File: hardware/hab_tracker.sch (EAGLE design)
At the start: 40 parts, among them IC1 LD117AV33, J3 GP-735T-VERTICAL, U1 ATMEGA328P_TQFP, U2 TMP102, U3 MPL3115A2, U4 9DoF IMU

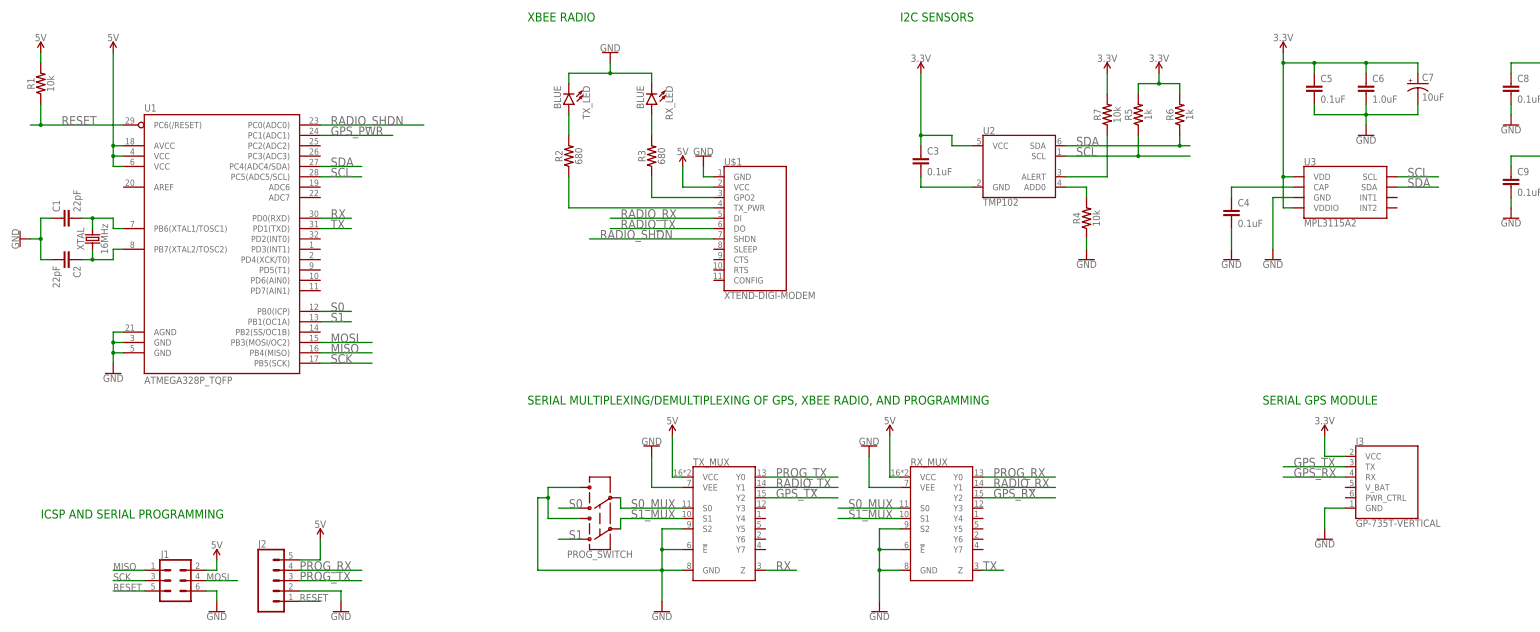
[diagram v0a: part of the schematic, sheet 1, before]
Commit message: Updated schematic and removed schematic history
Removed unnecessary schematic history files generated by Eagle. Also
changed from ATMEGA328p to ATMEGA2561. This allows for removal of serial
MUX circuitry as there are 2 UART ports on the ATMEGA2561 chip. This
will greatly simplify both the hardware and the firmware. Also, removed
serial programming capability. All programming will be done over JTAG
using AVR Pocket Programmer.
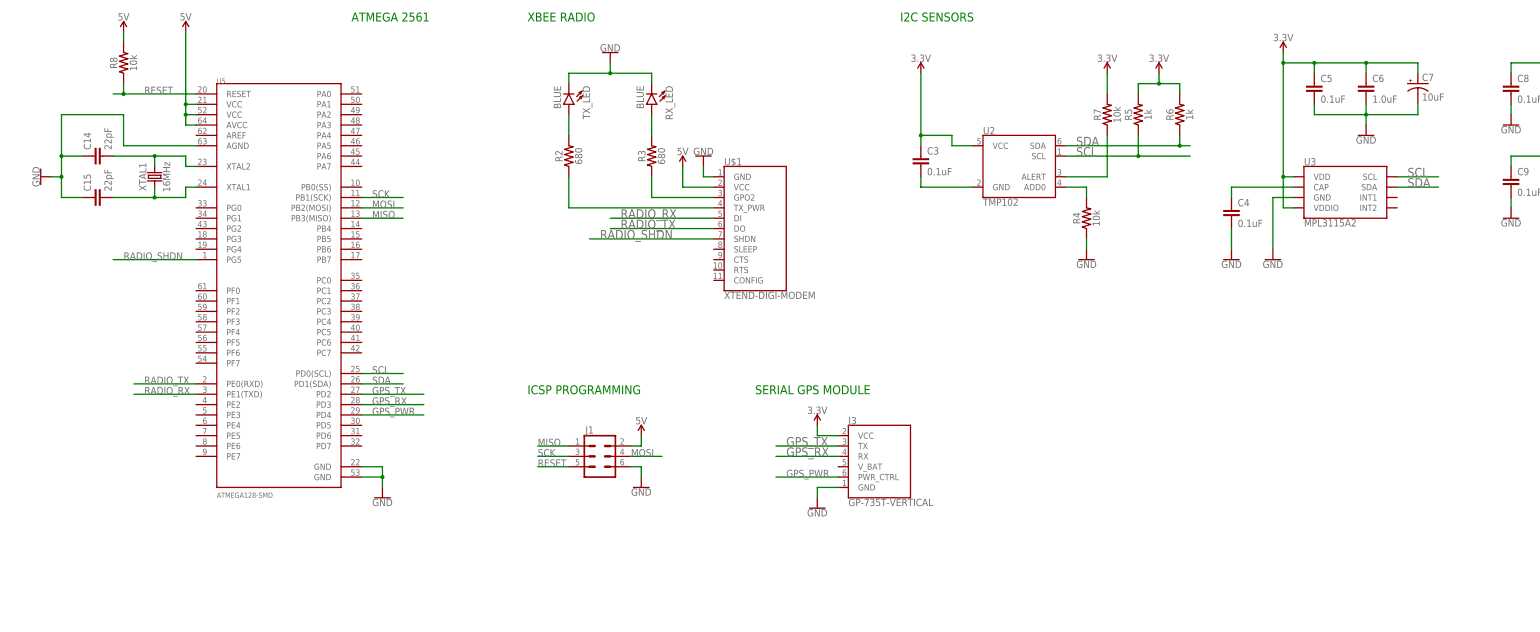
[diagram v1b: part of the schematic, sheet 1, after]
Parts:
- removed C1, C2: 22pF, SparkFun-Capacitors:22PF-0603-50V-5%
- removed J2: (no value), SparkFun-Connectors:CONN_05LOCK
- removed PROG_SWITCH: (no value), SparkFun-Switches:SWITCH-DPDT-SMD-AYZ0202
- removed R1: 10k, SparkFun-Resistors:10KOHM-0603-1/10W-1%
- removed RX_MUX, TX_MUX: (no value), SparkFun-IC-Logic:74HC4051BQ
- removed U1: ATMEGA328P_TQFP, SparkFun-IC-Microcontroller:ATMEGA328P_TQFP
- removed XTAL: 16MHz, SparkFun-Clocks:CRYSTAL-16MHZSMD-5X3.2
- added C14, C15: 22pF, SparkFun-Capacitors:22PF-0603-50V-5%
- added R8: 10k, SparkFun-Resistors:10KOHM-0603-1/10W-1%
- added U5: ATMEGA128-SMD, SparkFun-IC-Microcontroller:ATMEGA128-SMD
- added XTAL1: 16MHz, SparkFun-Clocks:CRYSTAL-16MHZSMD-5X3.2
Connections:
- removed net N$1: C1.2, U1.PB6(XTAL1/TOSC1), XTAL.2
- removed net N$2: C2.1, U1.PB7(XTAL2/TOSC2), XTAL.1
- removed net PROG_RX: J2.4, RX_MUX.Y0
- removed net PROG_TX: J2.3, TX_MUX.Y0
- removed net RX: TX_MUX.Z, U1.PD0(RXD)
- removed net S0: PROG_SWITCH.4, U1.PB0(ICP)
- removed net S0_MUX: PROG_SWITCH.5, RX_MUX.S0, TX_MUX.S0
- removed net S1: PROG_SWITCH.1, U1.PB1(OC1A)
- removed net S1_MUX: PROG_SWITCH.2, RX_MUX.S1, TX_MUX.S1
- removed net TX: RX_MUX.Z, U1.PD1(TXD)
- new net N$16: C14.2, U5.XTAL2, XTAL1.2
- new net N$17: C15.2, U5.XTAL1, XTAL1.1
- net 5V: now also R8.2, U5.AVCC, U5.VCC@21, U5.VCC@52; no longer J2.5, R1.2, RX_MUX.VCC, TX_MUX.VCC, U1.AVCC, U1.VCC@4, U1.VCC@6
- net GND: now also C14.1, C15.1, U5.AGND, U5.GND@22, U5.GND@53; no longer C1.1, C2.2, J2.2, PROG_SWITCH.3, PROG_SWITCH.6, RX_MUX.!E!, RX_MUX.GND, RX_MUX.S2, RX_MUX.VEE, TX_MUX.!E!, TX_MUX.GND, TX_MUX.S2, TX_MUX.VEE, U1.AGND, U1.GND@3, U1.GND@5
- net GPS_PWR: now also J3.PWR_CTRL, U5.PD4; no longer U1.PC1(ADC1)
- net GPS_RX: now also U5.PD3; no longer RX_MUX.Y2
- net GPS_TX: now also U5.PD2; no longer TX_MUX.Y2
- net MISO: now also U5.PB3(MISO); no longer U1.PB4(MISO)
- net MOSI: now also U5.PB2(MOSI); no longer U1.PB3(MOSI/OC2)
- net RADIO_RX: now also U5.PE1(TXD); no longer RX_MUX.Y1
- net RADIO_SHDN: now also U5.PG5; no longer U1.PC0(ADC0)
- net RADIO_TX: now also U5.PE0(RXD); no longer TX_MUX.Y1
- net RESET: now also R8.1, U5.RESET; no longer J2.1, R1.1, U1.PC6(/RESET)
- net SCK: now also U5.PB1(SCK); no longer U1.PB5(SCK)
- net SCL: now also U5.PD0(SCL); no longer U1.PC5(ADC5/SCL)
- net SDA: now also U5.PD1(SDA); no longer U1.PC4(ADC4/SDA)
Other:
- note added: "ATMEGA 2561"
- note added: "ICSP PROGRAMMING"
- note removed: "ICSP AND SERIAL PROGRAMMING"
- note removed: "SERIAL MULTIPLEXING/DEMULTIPLEXING OF GPS, XBEE RADIO, AND PROGRAMMING"
- moved on the sheet: J1, J3
